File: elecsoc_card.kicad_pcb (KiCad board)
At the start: 2 copper layers, 88 x 50 mm, 22 parts, among them J1 Conn_01x02_Pin, J2 Conn_01x02_Pin, U1 NA555D

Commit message: Removed Items for Rev2, for Daniel to complete
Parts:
- removed J2: Conn_01x02_Pin, Library:USB_A_Male_inboard
- C1: value 47u -> 10u
- R1, R2: value 4k99 -> 50k
- R3, R4, R5, R6, R7: value 392 -> 390
- moved R10 46.7 mm to (158.7, 95.6)
- moved D8 19.3 mm to (158.7, 91.0)
- moved R9 17.7 mm to (153.2, 95.6)
- moved D6 14.5 mm to (144.2, 91.0), turned to 90 degrees
- moved R8 13.8 mm to (144.2, 95.6)
- moved R1 8.95 mm to (168.1, 63.7), turned to 0 degrees
- moved R2 8.94 mm to (168.9, 67.1), turned to -90 degrees
- moved C1 6.03 mm to (168.9, 71.3)
- moved U1 4.88 mm to (163.7, 68.0), turned to 0 degrees
- moved D7 4.23 mm to (153.2, 91.0), turned to 90 degrees
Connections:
- D6 pad 1: GND -> Net-(D6-K)
- D6 pad 2: Net-(D6-A) -> /555 Output
- D7 pad 1: GND -> Net-(D7-K)
- D7 pad 2: Net-(D7-A) -> /555 Output
- D8 pad 1: GND -> Net-(D8-K)
- D8 pad 2: Net-(D8-A) -> /555 Output
- R10 pad 1: /555 Output -> Net-(D8-K)
- R10 pad 2: Net-(D8-A) -> GND
- R8 pad 1: /555 Output -> Net-(D6-K)
- R8 pad 2: Net-(D6-A) -> GND
- R9 pad 1: /555 Output -> Net-(D7-K)
- R9 pad 2: Net-(D7-A) -> GND
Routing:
- net /555 Output: track 142.0 -> 1.09 mm, vias 12 -> 0
- net GND: track 59.6 -> 0.63 mm, vias 3 -> 0
- net Net-(D8-A): track 32.5 -> 0.00 mm, vias 2 -> 0
- net +5V: track 73.6 -> 44.1 mm, vias 1 -> 0
- net Net-(D7-A): track 15.6 -> 0.00 mm, vias 2 -> 0
- net Net-(U1-THR): track 14.6 -> 0.00 mm, vias 2 -> 0
- net Net-(D6-A): track 13.0 -> 0.00 mm, vias 2 -> 0
- net Net-(U1-DIS): track 9.08 -> 0.00 mm
- removed copper zone on F.Cu, net GND

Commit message: Routing added
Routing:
- net /555 Output: track 1.09 -> 93.1 mm, vias 0 -> 6
- net GND: track 0.63 -> 71.3 mm, vias 0 -> 2
- net +5V: track 44.1 -> 67.1 mm, vias 0 -> 2
- net Net-(U1-THR): track 0.00 -> 10.6 mm
- net Net-(U1-DIS): track 0.00 -> 5.73 mm
- net Net-(D8-K): track 0.00 -> 2.55 mm
- net Net-(D7-K): track 0.00 -> 2.55 mm
- net Net-(D6-K): track 0.00 -> 2.55 mm
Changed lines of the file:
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@@
     (effects (font (size 2 2) (thickness 0.5) bold) (justify left bottom mirror))
   )
+  (segment (start 166.2 68.64) (end 168.39 68.64) (width 0.25) (layer "F.Cu") (net 1))
+  (segment (start 166.2 68.64) (end 165.575 68.015) (width 0.25) (layer "F.Cu") (net 1))
+  (segment (start 161.895 68.015) (end 161.25 67.37) (width 0.25) (layer "F.Cu") (net 1))
+  (segment (start 165.575 68.015) (end 161.895 68.015) (width 0.25) (layer "F.Cu") (net 1))
+  (segment (start 168.39 68.64) (end 168.925 68.105) (width 0.25) (layer "F.Cu") (net 1))
+  (segment (start 168.925 70.2675) (end 168.925 68.105) (width 0.25) (layer "F.Cu") (net 1))
+  (segment (start 166.3425 72.3425) (end 165.8 71.8) (width 0.25) (layer "F.Cu") (net 2))
+  (segment (start 161.2 66.05) (end 161.25 66.1) (width 0.25) (layer "F.Cu") (net 2))
+  (segment (start 162.4 96.6) (end 164.8 94.2) (width 0.25) (layer "F.Cu") (net 2))
   (segment (start 177.62247 65.527279) (end 176.996949 65.527279) (width 0.25) (layer "F.Cu") (net 2))
+  (segment (start 170.807249 72.3425) (end 177.62247 65.527279) (width 0.25) (layer "F.Cu") (net 2))
+  (segment (start 161.2 64.4) (end 161.2 66.05) (width 0.25) (layer "F.Cu") (net 2))
+  (segment (start 164.8 94.2) (end 164.8 72.8) (width 0.25) (layer "F.Cu") (net 2))
+  (segment (start 144.2 96.6) (end 153.2 96.6) (width 0.25) (layer "F.Cu") (net 2))
+  (segment (start 158.7 96.6) (end 162.4 96.6) (width 0.25) (layer "F.Cu") (net 2))
+  (segment (start 168.925 72.3425) (end 166.3425 72.3425) (width 0.25) (layer "F.Cu") (net 2))
+  (segment (start 168.925 72.3425) (end 170.807249 72.3425) (width 0.25) (layer "F.Cu") (net 2))
+  (segment (start 153.2 96.6) (end 158.7 96.6) (width 0.25) (layer "F.Cu") (net 2))
+  (segment (start 164.8 72.8) (end 165.8 71.8) (width 0.25) (layer "F.Cu") (net 2))
+  (via (at 161.2 64.4) (size 0.8) (drill 0.4) (layers "F.Cu" "B.Cu") (net 2))
+  (via (at 165.8 71.8) (size 0.8) (drill 0.4) (layers "F.Cu" "B.Cu") (net 2))
+  (segment (start 165.8 71.8) (end 165.174695 71.8) (width 0.25) (layer "B.Cu") (net 2))
+  (segment (start 161.2 67.825305) (end 161.2 64.4) (width 0.25) (layer "B.Cu") (net 2))
+  (segment (start 165.174695 71.8) (end 161.2 67.825305) (width 0.25) (layer "B.Cu") (net 2))
+  (segment (start 112.3 79.2) (end 122.8 79.2) (width 0.25) (layer "F.Cu") (net 3))
+  (segment (start 158.9355 68.64) (end 158.8 68.7755) (width 0.25) (layer "F.Cu") (net 3))
+  (segment (start 144.475 83.325) (end 144.4 83.4) (width 0.25) (layer "F.Cu") (net 3))
+  (segment (start 144.3 80.2) (end 144.475 80.025) (width 0.25) (layer "F.Cu") (net 3))
+  (segment (start 126.15 79.2) (end 133.3 79.2) (width 0.25) (layer "F.Cu") (net 3))
+  (segment (start 111.975 79.525) (end 112.3 79.2) (width 0.25) (layer "F.Cu") (net 3))
+  (segment (start 155.475 83.125) (end 155.4 83.2) (width 0.25) (layer "F.Cu") (net 3))
   (segment (start 133.475 79.025) (end 134.025 79.025) (width 0.25) (layer "F.Cu") (net 3))
-  (segment (start 111.975 79.525) (end 112 79.5) (width 0.25) (layer "F.Cu") (net 3))
+  (segment (start 134 80.2) (end 144.3 80.2) (width 0.25) (layer "F.Cu") (net 3))
+  (segment (start 144.475 80.025) (end 144.475 83.325) (width 0.25) (layer "F.Cu") (net 3))
+  (segment (start 144 89.8) (end 144.2 90) (width 0.25) (layer "F.Cu") (net 3))
+  (segment (start 161.25 68.64) (end 158.9355 68.64) (width 0.25) (layer "F.Cu") (net 3))
+  (segment (start 142 89.8) (end 144 89.8) (width 0.25) (layer "F.Cu") (net 3))
+  (segment (start 155.475 81.025) (end 155.475 83.125) (width 0.25) (layer "F.Cu") (net 3))
   (segment (start 123.975 77.525) (end 124.475 77.525) (width 0.25) (layer "F.Cu") (net 3))
+  (segment (start 153.2 90) (end 158.7 90) (width 0.25) (layer "F.Cu") (net 3))
+  (segment (start 151.4 90) (end 153.2 90) (width 0.25) (layer "F.Cu") (net 3))
+  (segment (start 133.3 79.2) (end 133.475 79.025) (width 0.25) (layer "F.Cu") (net 3))
+  (segment (start 144.2 90) (end 146.6 90) (width 0.25) (layer "F.Cu") (net 3))
+  (segment (start 133.475 79.025) (end 133.475 79.675) (width 0.25) (layer "F.Cu") (net 3))
+  (segment (start 144.475 80.025) (end 144.2 80.3) (width 0.25) (layer "F.Cu") (net 3))
+  (segment (start 124.475 77.525) (end 126.15 79.2) (width 0.25) (layer "F.Cu") (net 3))
+  (segment (start 122.8 79.2) (end 124.475 77.525) (width 0.25) (layer "F.Cu") (net 3))
+  (segment (start 133.475 79.675) (end 134 80.2) (width 0.25) (layer "F.Cu") (net 3))
+  (via (at 158.8 68.7755) (size 0.8) (drill 0.4) (layers "F.Cu" "B.Cu") (net 3))
+  (via (at 155.4 83.2) (size 0.8) (drill 0.4) (layers "F.Cu" "B.Cu") (net 3))
+  (via (at 142 89.8) (size 0.8) (drill 0.4) (layers "F.Cu" "B.Cu") (net 3))
+  (via (at 146.6 90) (size 0.8) (drill 0.4) (layers "F.Cu" "B.Cu") (net 3))
+  (via (at 151.4 90) (size 0.8) (drill 0.4) (layers "F.Cu" "B.Cu") (net 3))
+  (via (at 144.4 83.4) (size 0.8) (drill 0.4) (layers "F.Cu" "B.Cu") (net 3))
+  (segment (start 146.6 90) (end 151.4 90) (width 0.25) (layer "B.Cu") (net 3))
+  (segment (start 144.4 83.4) (end 144.4 87.4) (width 0.25) (layer "B.Cu") (net 3))
+  (segment (start 155.4 86) (end 151.4 90) (width 0.25) (layer "B.Cu") (net 3))
+  (segment (start 158.8 68.7755) (end 158.8 79.8) (width 0.25) (layer "B.Cu") (net 3))
+  (segment (start 158.8 79.8) (end 155.4 83.2) (width 0.25) (layer "B.Cu") (net 3))
+  (segment (start 155.4 83.2) (end 155.4 86) (width 0.25) (layer "B.Cu") (net 3))
+  (segment (start 144.4 87.4) (end 142 89.8) (width 0.25) (layer "B.Cu") (net 3))
   (segment (start 112 77.45) (end 111.975 77.475) (width 0.25) (layer "F.Cu") (net 4))
   (segment (start 112 71.5) (end 112 77.45) (width 0.25) (layer "F.Cu") (net 4))
@@
   (segment (start 144.5 71.5) (end 144.5 77.95) (width 0.25) (layer "F.Cu") (net 8))
   (segment (start 144.5 77.95) (end 144.475 77.975) (width 0.25) (layer "F.Cu") (net 8))
+  (segment (start 144.2 92.05) (end 144.2 94.6) (width 0.25) (layer "F.Cu") (net 9))
+  (segment (start 153.2 94.6) (end 153.2 92.05) (width 0.25) (layer "F.Cu") (net 10))
+  (segment (start 158.7 94.6) (end 158.7 92.05) (width 0.25) (layer "F.Cu") (net 11))
+  (segment (start 170.252469 60.577531) (end 172.672722 60.577531) (width 0.25) (layer "F.Cu") (net 12))
+  (segment (start 160.84 69.5) (end 155.5 69.5) (width 0.25) (layer "F.Cu") (net 12))
   (segment (start 112 69.5) (end 156 69.5) (width 0.25) (layer "F.Cu") (net 12))
+  (segment (start 161.25 69.91) (end 162.49 69.91) (width 0.25) (layer "F.Cu") (net 12))
+  (segment (start 165.7 66.6) (end 166.2 66.1) (width 0.25) (layer "F.Cu") (net 12))
+  (segment (start 167.125 63.705) (end 170.252469 60.577531) (width 0.25) (layer "F.Cu") (net 12))
+  (segment (start 164.2 66.6) (end 165.7 66.6) (width 0.25) (layer "F.Cu") (net 12))
+  (segment (start 166.2 66.1) (end 166.2 64.63) (width 0.25) (layer "F.Cu") (net 12))
   (segment (start 155.5375 69.4625) (end 155.5 69.5) (width 0.25) (layer "F.Cu") (net 12))
+  (segment (start 162.49 69.91) (end 163.4 69) (width 0.25) (layer "F.Cu") (net 12))
   (segment (start 172.672722 60.627278) (end 172.672722 60.577531) (width 0.25) (layer "F.Cu") (net 12))
+  (segment (start 161.25 69.91) (end 160.84 69.5) (width 0.25) (layer "F.Cu") (net 12))
+  (segment (start 166.2 64.63) (end 167.125 63.705) (width 0.25) (layer "F.Cu") (net 12))
+  (via (at 163.4 69) (size 0.8) (drill 0.4) (layers "F.Cu" "B.Cu") (net 12))
+  (via (at 164.2 66.6) (size 0.8) (drill 0.4) (layers "F.Cu" "B.Cu") (net 12))
+  (segment (start 163.4 69) (end 164.2 68.2) (width 0.25) (layer "B.Cu") (net 12))
+  (segment (start 164.2 68.2) (end 164.2 66.6) (width 0.25) (layer "B.Cu") (net 12))
+  (segment (start 169.125 65.905) (end 168.925 66.105) (width 0.25) (layer "F.Cu") (net 13))
+  (segment (start 168.925 66.105) (end 167.66 67.37) (width 0.25) (layer "F.Cu") (net 13))
+  (segment (start 167.66 67.37) (end 166.2 67.37) (width 0.25) (layer "F.Cu") (net 13))
+  (segment (start 169.125 63.705) (end 169.125 65.905) (width 0.25) (layer "F.Cu") (net 13))
   (zone (net 0) (net_name "") (layers "F&B.Cu") (hatch edge 0.5)
     (connect_pads (clearance 0))

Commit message: Added silkscreen on usb port
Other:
- board text added: "+5V"
- board text added: "GND"
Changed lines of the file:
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@@
     (effects (font (size 2 2) (thickness 0.4)) (justify left bottom))
+  )
+  (gr_text "GND\n" (at 172.6 65.8) (layer "F.SilkS")
+    (effects (font (size 1 1) (thickness 0.15)) (justify left bottom))
+  )
+  (gr_text "+5V" (at 167.4 60.2) (layer "F.SilkS")
+    (effects (font (size 1 1) (thickness 0.15)) (justify left bottom))
   )
   (gr_text "Since 1990" (at 105 63) (layer "F.SilkS")

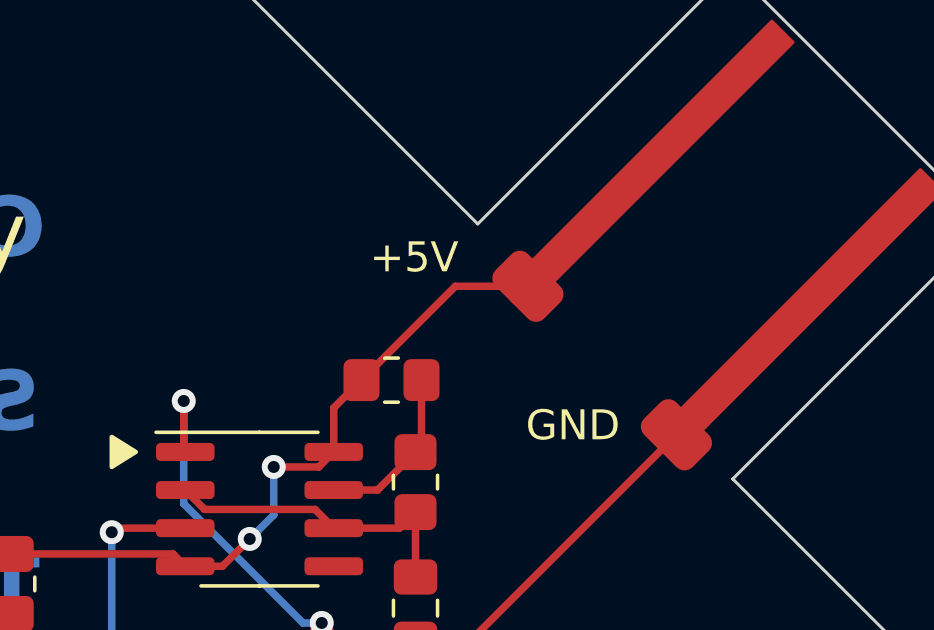
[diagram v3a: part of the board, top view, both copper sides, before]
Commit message: Protection resistor and capacitor + cut for 3d printed part
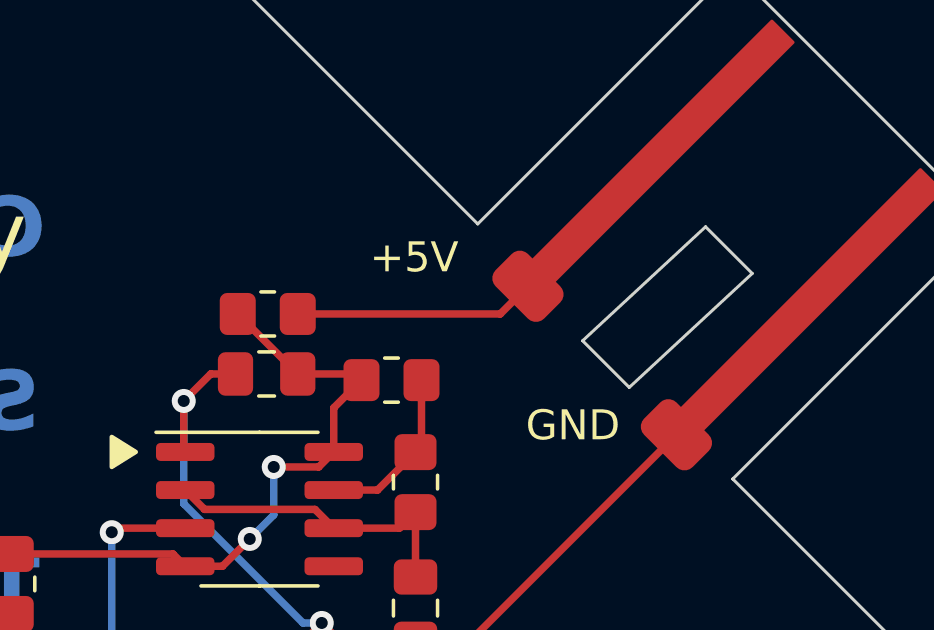
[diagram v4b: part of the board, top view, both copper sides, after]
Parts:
- added C2: 10u, Capacitor_SMD:C_0805_2012Metric_Pad1.18x1.45mm_HandSolder, F.Cu at (164.0, 63.5)
- added R11: 5, Resistor_SMD:R_0805_2012Metric_Pad1.20x1.40mm_HandSolder, F.Cu at (164.0, 61.5)
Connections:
- J1 pad 1: +5V -> Net-(J1-Pin_1)
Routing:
- net Net-(J1-Pin_1): track 0.00 -> 8.10 mm
- net GND: track 71.3 -> 73.4 mm
- net +5V: track 67.1 -> 65.3 mm
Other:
- outline, holes or cut-outs redrawn

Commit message: Manufacturer files
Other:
- board text removed: "+5V"
- board text removed: "GND"
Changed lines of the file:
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@@
     (fp_line (start 1 0.625) (end -1 0.625)
       (stroke (width 0.1) (type solid)) (layer "F.Fab"))
-    (pad "1" smd roundrect (at -1 0) (size 1.2 1.4) (layers "F.Cu" "F.Paste" "F.Mask") (roundrect_rratio 0.208333)
+    (pad "1" smd roundrect (at -1 0) (size 1.2 1.4) (layers "F.Cu" "F.Paste" "F.Mask") (roundrect_rratio 0.2083333333)
       (net 12 "+5V") (pintype "passive"))
-    (pad "2" smd roundrect (at 1 0) (size 1.2 1.4) (layers "F.Cu" "F.Paste" "F.Mask") (roundrect_rratio 0.208333)
+    (pad "2" smd roundrect (at 1 0) (size 1.2 1.4) (layers "F.Cu" "F.Paste" "F.Mask") (roundrect_rratio 0.2083333333)
       (net 15 "Net-(J1-Pin_1)") (pintype "passive"))
     (model "${KICAD6_3DMODEL_DIR}/Resistor_SMD.3dshapes/R_0805_2012Metric.wrl"
@@
     (fp_line (start 1 0.625) (end -1 0.625)
       (stroke (width 0.1) (type solid)) (layer "F.Fab"))
-    (pad "1" smd roundrect (at -1.0375 0 180) (size 1.175 1.45) (layers "F.Cu" "F.Paste" "F.Mask") (roundrect_rratio 0.212766)
+    (pad "1" smd roundrect (at -1.0375 0 180) (size 1.175 1.45) (layers "F.Cu" "F.Paste" "F.Mask") (roundrect_rratio 0.2127659574)
       (net 12 "+5V") (pintype "passive"))
-    (pad "2" smd roundrect (at 1.0375 0 180) (size 1.175 1.45) (layers "F.Cu" "F.Paste" "F.Mask") (roundrect_rratio 0.212766)
+    (pad "2" smd roundrect (at 1.0375 0 180) (size 1.175 1.45) (layers "F.Cu" "F.Paste" "F.Mask") (roundrect_rratio 0.2127659574)
       (net 2 "GND") (pintype "passive"))
     (model "${KICAD6_3DMODEL_DIR}/Capacitor_SMD.3dshapes/C_0805_2012Metric.wrl"
@@
     (fp_line (start 1 0.625) (end -1 0.625)
       (stroke (width 0.1) (type solid)) (layer "F.Fab"))
-    (pad "1" smd roundrect (at -1 0 270) (size 1.2 1.4) (layers "F.Cu" "F.Paste" "F.Mask") (roundrect_rratio 0.208333)
+    (pad "1" smd roundrect (at -1 0 270) (size 1.2 1.4) (layers "F.Cu" "F.Paste" "F.Mask") (roundrect_rratio 0.2083333333)
       (net 9 "Net-(D6-K)") (pintype "passive"))
-    (pad "2" smd roundrect (at 1 0 270) (size 1.2 1.4) (layers "F.Cu" "F.Paste" "F.Mask") (roundrect_rratio 0.208333)
+    (pad "2" smd roundrect (at 1 0 270) (size 1.2 1.4) (layers "F.Cu" "F.Paste" "F.Mask") (roundrect_rratio 0.2083333333)
       (net 2 "GND") (pintype "passive"))
     (model "${KICAD6_3DMODEL_DIR}/Resistor_SMD.3dshapes/R_0805_2012Metric.wrl"
@@
     (fp_line (start 1 0.6) (end 1 -0.6)
       (stroke (width 0.1) (type solid)) (layer "F.Fab"))
-    (pad "1" smd roundrect (at -1.025 0 90) (size 1.15 1.4) (layers "F.Cu" "F.Paste" "F.Mask") (roundrect_rratio 0.217391)
+    (pad "1" smd roundrect (at -1.025 0 90) (size 1.15 1.4) (layers "F.Cu" "F.Paste" "F.Mask") (roundrect_rratio 0.2173913043)
       (net 11 "Net-(D8-K)") (pinfunction "K") (pintype "passive"))
-    (pad "2" smd roundrect (at 1.025 0 90) (size 1.15 1.4) (layers "F.Cu" "F.Paste" "F.Mask") (roundrect_rratio 0.217391)
+    (pad "2" smd roundrect (at 1.025 0 90) (size 1.15 1.4) (layers "F.Cu" "F.Paste" "F.Mask") (roundrect_rratio 0.2173913043)
       (net 3 "/555 Output") (pinfunction "A") (pintype "passive"))
     (model "${KICAD6_3DMODEL_DIR}/LED_SMD.3dshapes/LED_0805_2012Metric.wrl"
@@
     (fp_line (start 1 0.6) (end 1 -0.6)
       (stroke (width 0.1) (type solid)) (layer "F.Fab"))
-    (pad "1" smd roundrect (at -1.025 0 90) (size 1.15 1.4) (layers "F.Cu" "F.Paste" "F.Mask") (roundrect_rratio 0.217391)
+    (pad "1" smd roundrect (at -1.025 0 90) (size 1.15 1.4) (layers "F.Cu" "F.Paste" "F.Mask") (roundrect_rratio 0.2173913043)
       (net 10 "Net-(D7-K)") (pinfunction "K") (pintype "passive"))
-    (pad "2" smd roundrect (at 1.025 0 90) (size 1.15 1.4) (layers "F.Cu" "F.Paste" "F.Mask") (roundrect_rratio 0.217391)
+    (pad "2" smd roundrect (at 1.025 0 90) (size 1.15 1.4) (layers "F.Cu" "F.Paste" "F.Mask") (roundrect_rratio 0.2173913043)
       (net 3 "/555 Output") (pinfunction "A") (pintype "passive"))
     (model "${KICAD6_3DMODEL_DIR}/LED_SMD.3dshapes/LED_0805_2012Metric.wrl"
@@
     (fp_line (start 1 0.6) (end 1 -0.6)
       (stroke (width 0.1) (type solid)) (layer "F.Fab"))
-    (pad "1" smd roundrect (at -1.025 0 90) (size 1.15 1.4) (layers "F.Cu" "F.Paste" "F.Mask") (roundrect_rratio 0.217391)
+    (pad "1" smd roundrect (at -1.025 0 90) (size 1.15 1.4) (layers "F.Cu" "F.Paste" "F.Mask") (roundrect_rratio 0.2173913043)
       (net 9 "Net-(D6-K)") (pinfunction "K") (pintype "passive"))
-    (pad "2" smd roundrect (at 1.025 0 90) (size 1.15 1.4) (layers "F.Cu" "F.Paste" "F.Mask") (roundrect_rratio 0.217391)
+    (pad "2" smd roundrect (at 1.025 0 90) (size 1.15 1.4) (layers "F.Cu" "F.Paste" "F.Mask") (roundrect_rratio 0.2173913043)
       (net 3 "/555 Output") (pinfunction "A") (pintype "passive"))
     (model "${KICAD6_3DMODEL_DIR}/LED_SMD.3dshapes/LED_0805_2012Metric.wrl"
@@
     (fp_line (start 1 0.625) (end -1 0.625)
       (stroke (width 0.1) (type solid)) (layer "F.Fab"))
-    (pad "1" smd roundrect (at -1 0 270) (size 1.2 1.4) (layers "F.Cu" "F.Paste" "F.Mask") (roundrect_rratio 0.208333)
+    (pad "1" smd roundrect (at -1 0 270) (size 1.2 1.4) (layers "F.Cu" "F.Paste" "F.Mask") (roundrect_rratio 0.2083333333)
       (net 11 "Net-(D8-K)") (pintype "passive"))
-    (pad "2" smd roundrect (at 1 0 270) (size 1.2 1.4) (layers "F.Cu" "F.Paste" "F.Mask") (roundrect_rratio 0.208333)
+    (pad "2" smd roundrect (at 1 0 270) (size 1.2 1.4) (layers "F.Cu" "F.Paste" "F.Mask") (roundrect_rratio 0.2083333333)
       (net 2 "GND") (pintype "passive"))
     (model "${KICAD6_3DMODEL_DIR}/Resistor_SMD.3dshapes/R_0805_2012Metric.wrl"
@@
     (fp_line (start 1 0.625) (end -1 0.625)
       (stroke (width 0.1) (type solid)) (layer "F.Fab"))
-    (pad "1" smd roundrect (at -1 0 270) (size 1.2 1.4) (layers "F.Cu" "F.Paste" "F.Mask") (roundrect_rratio 0.208333)
+    (pad "1" smd roundrect (at -1 0 270) (size 1.2 1.4) (layers "F.Cu" "F.Paste" "F.Mask") (roundrect_rratio 0.2083333333)
       (net 10 "Net-(D7-K)") (pintype "passive"))
-    (pad "2" smd roundrect (at 1 0 270) (size 1.2 1.4) (layers "F.Cu" "F.Paste" "F.Mask") (roundrect_rratio 0.208333)
+    (pad "2" smd roundrect (at 1 0 270) (size 1.2 1.4) (layers "F.Cu" "F.Paste" "F.Mask") (roundrect_rratio 0.2083333333)
       (net 2 "GND") (pintype "passive"))
     (model "${KICAD6_3DMODEL_DIR}/Resistor_SMD.3dshapes/R_0805_2012Metric.wrl"
@@
     (effects (font (size 2 2) (thickness 0.4)) (justify left bottom))
   )
-  (gr_text "GND\n" (at 172.6 65.8) (layer "F.SilkS")
-    (effects (font (size 1 1) (thickness 0.15)) (justify left bottom))
-  )
-  (gr_text "+5V" (at 167.4 60.2) (layer "F.SilkS")
-    (effects (font (size 1 1) (thickness 0.15)) (justify left bottom))
-  )
   (gr_text "Since 1990" (at 105 63) (layer "F.SilkS")
